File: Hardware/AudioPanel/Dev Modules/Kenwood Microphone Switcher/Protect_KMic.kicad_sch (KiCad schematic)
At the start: 28 parts

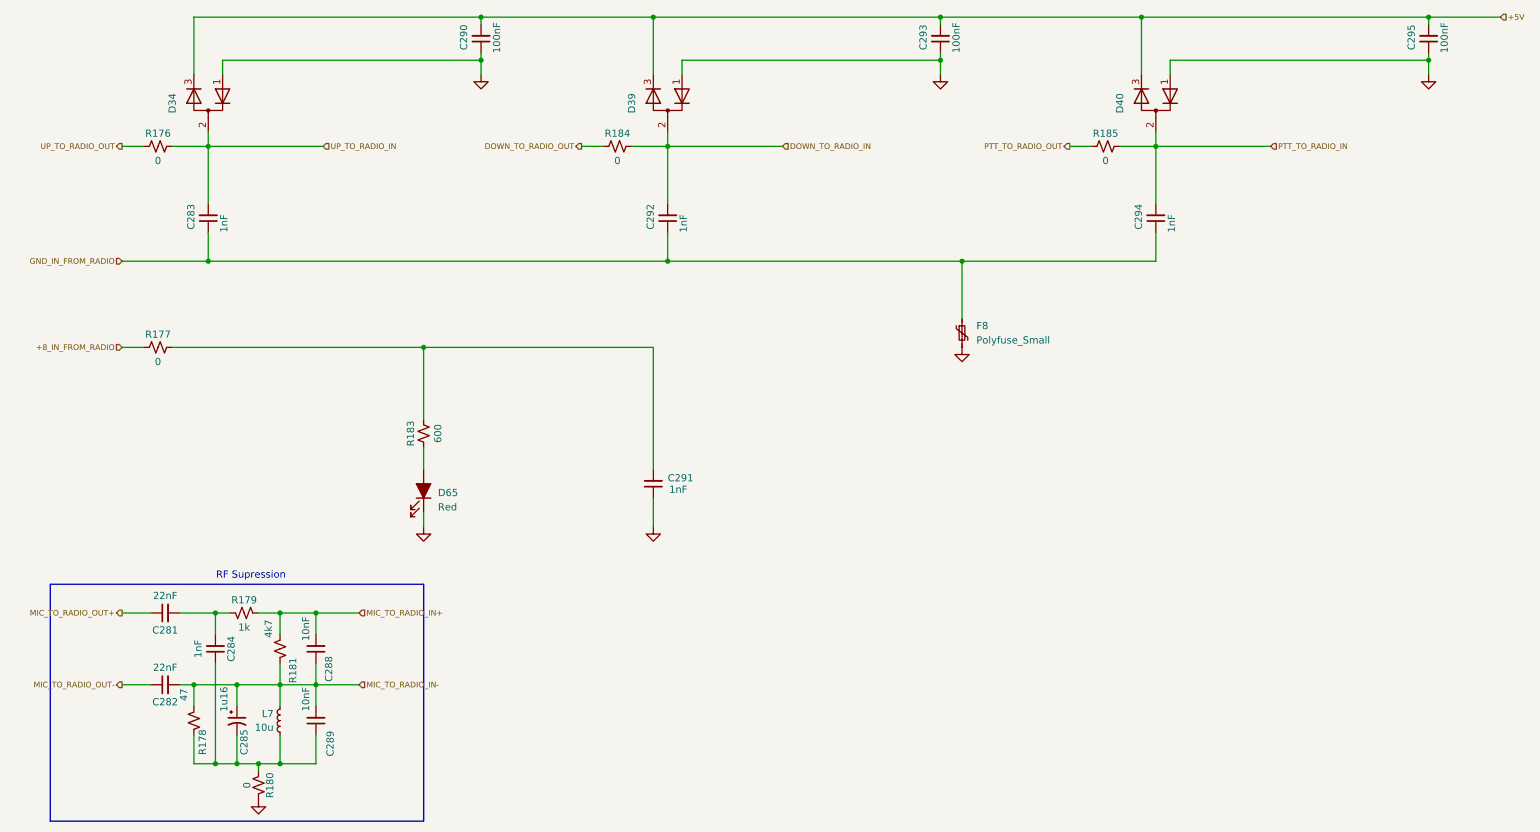
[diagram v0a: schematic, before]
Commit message: Added microphone switcher initial schematic
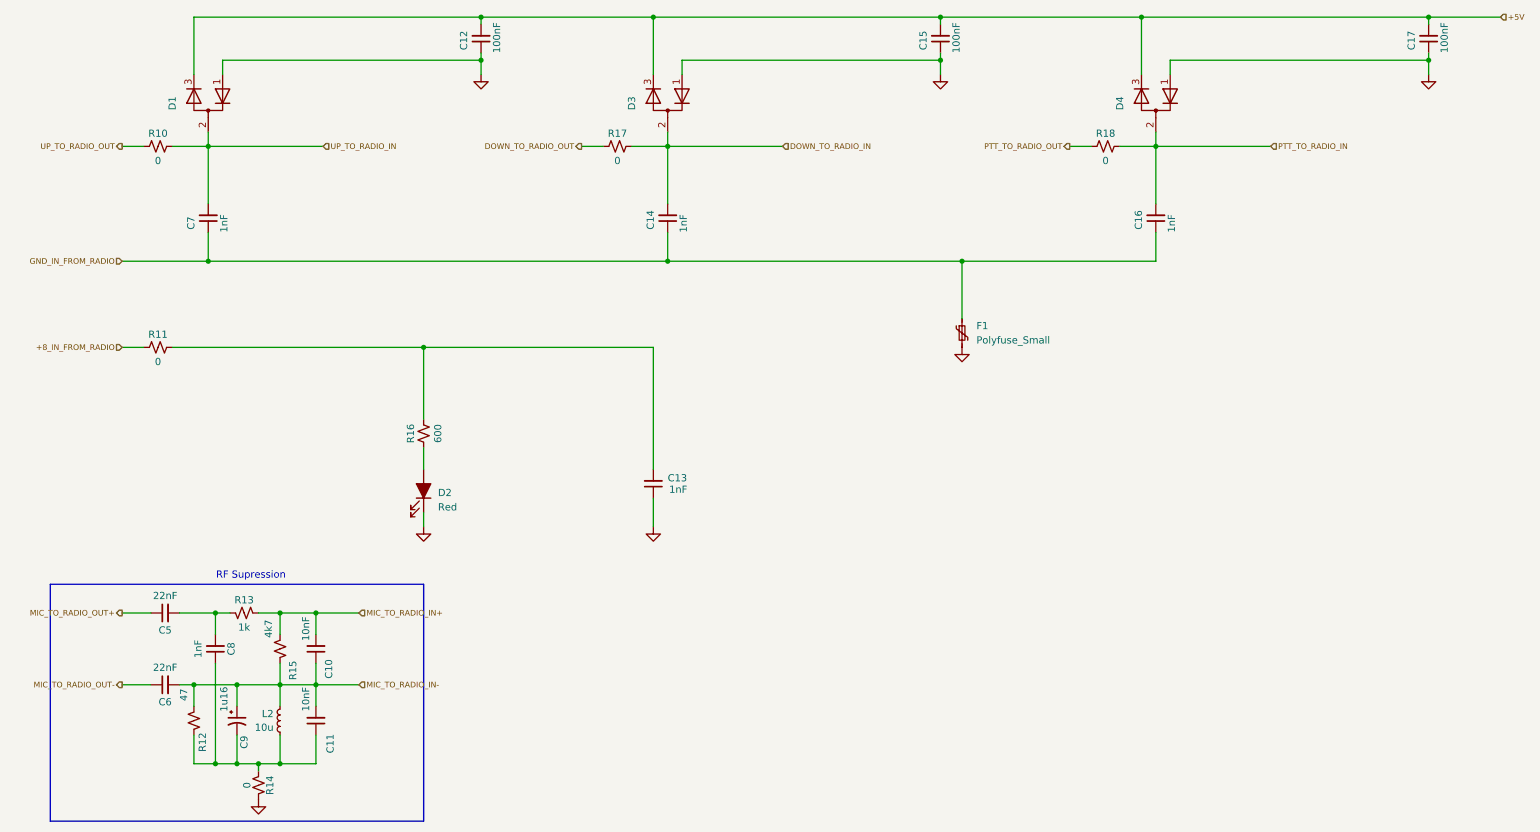
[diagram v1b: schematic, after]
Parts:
- renumbered C288 to C10, C289 to C11, C290 to C12, C291 to C13, C292 to C14, C293 to C15, C294 to C16, C295 to C17, C281 to C5, C282 to C6, C283 to C7, C284 to C8, C285 to C9, D34 to D1, D65 to D2, D39 to D3, D40 to D4, F8 to F1, L7 to L2, R176 to R10, R177 to R11, R178 to R12, R179 to R13, R180 to R14, R181 to R15, R183 to R16, R184 to R17, R185 to R18
